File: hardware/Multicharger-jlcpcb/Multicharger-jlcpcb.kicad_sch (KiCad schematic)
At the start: 27 parts, among them J101 Conn_01x02, J102 Conn_01x02, J103 Tagbase, J104 USB_B_Mini, SW101 SW_DIP_x04, U101 TPS3700, U106 XC6206-3.3V

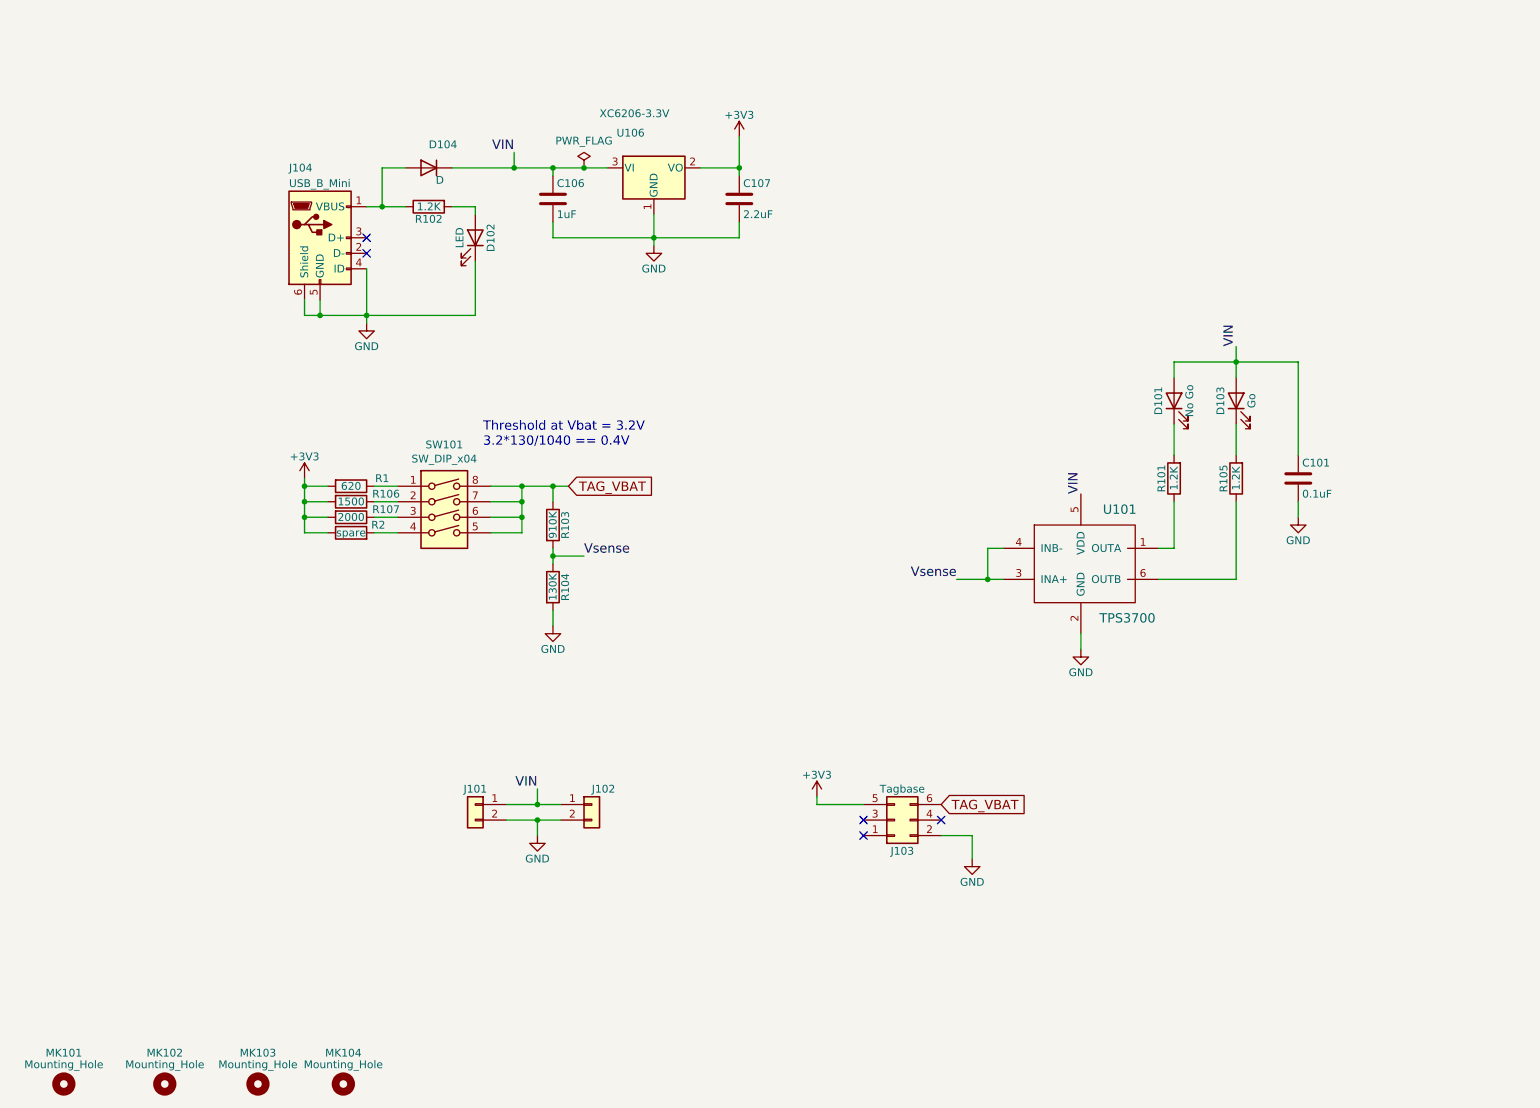
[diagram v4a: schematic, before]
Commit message: update multicharger to use basic parts
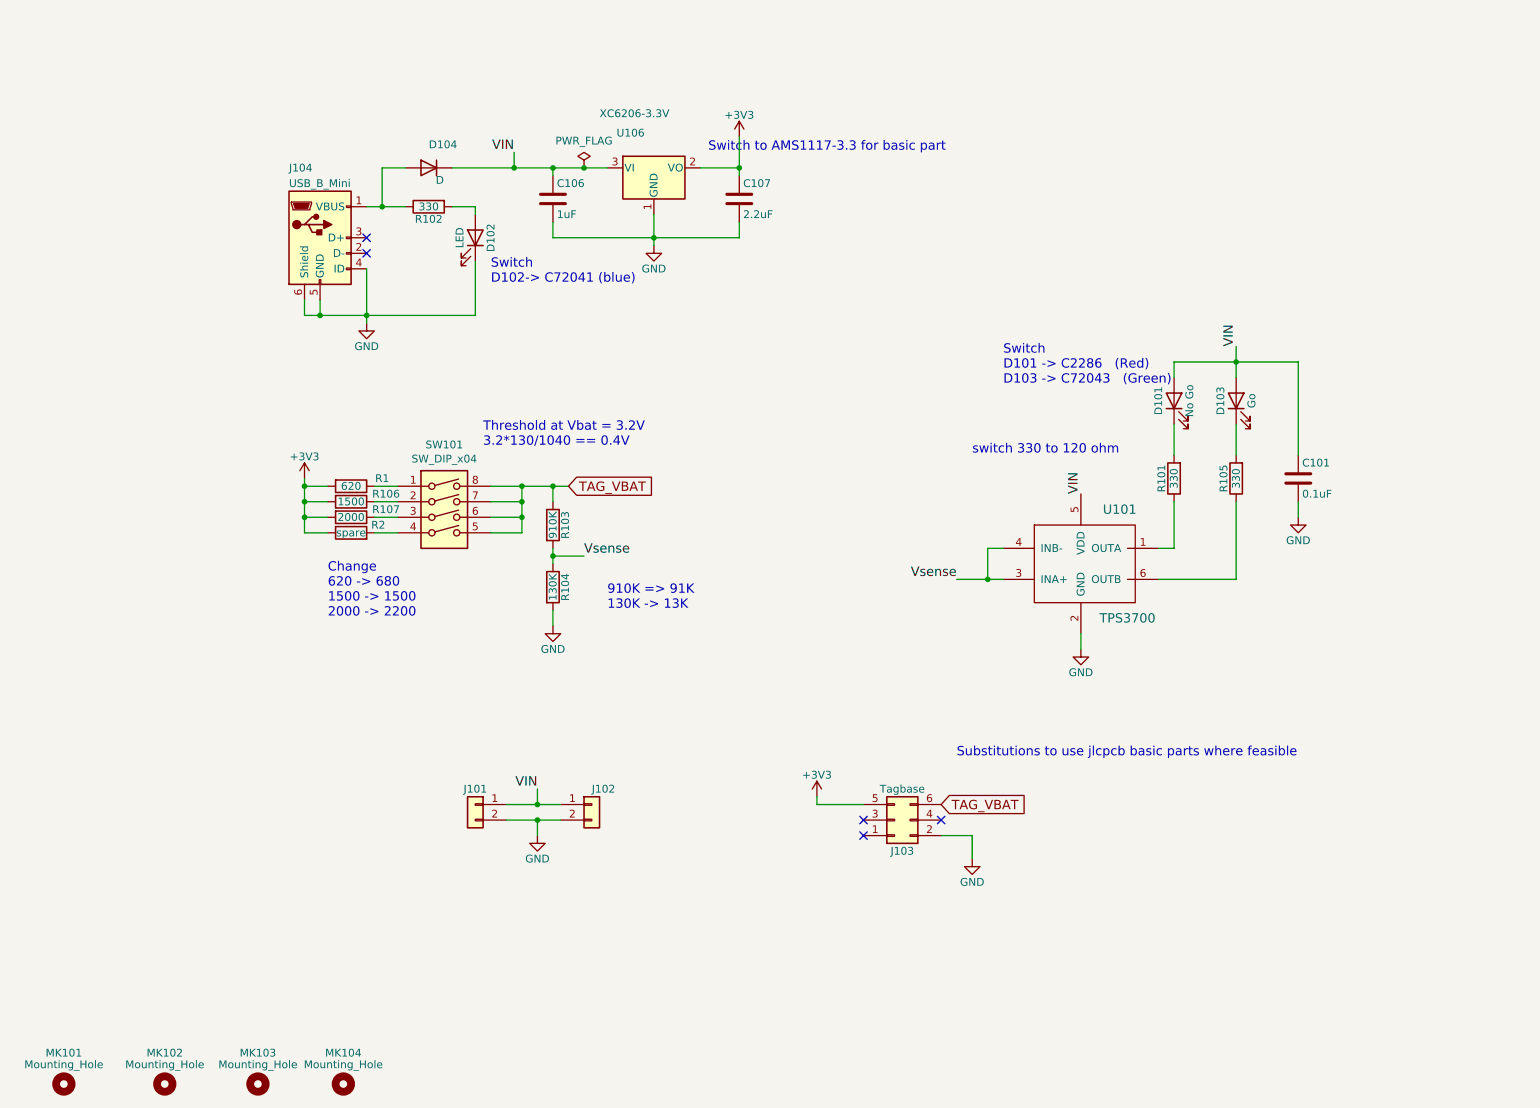
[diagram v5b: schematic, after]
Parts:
- R101, R102, R105: value 1.2K -> 330; LCSC C114605 -> C23138; MFN Yaego -> Uniroyal; MPN RC0603FR-071K2L -> 0603WAF3300T5E
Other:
- note added: "910K => 91K 130K -> 13K"
- note added: "Change 620 -> 680 1500 -> 1500 2000 -> 2200"
- note added: "Substitutions to use jlcpcb basic parts where feasible"
- note added: "Switch D101 -> C2286 (Red) D103 -> C72043 (Green)"
- note added: "Switch D102-> C72041 (blue)"
- note added: "Switch to AMS1117-3.3 for basic part"
- note added: "switch 330 to 120 ohm"
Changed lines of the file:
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@@
     (stroke (width 0) (type default) (color 0 0 0 0))
   )
+  (text "910K => 91K\n130K -> 13K" (at 125.73 114.3 0)
+    (effects (font (size 1.524 1.524)) (justify left bottom))
+  )
+  (text "Switch\nD102-> C72041 (blue)" (at 106.68 60.96 0)
+    (effects (font (size 1.524 1.524)) (justify left bottom))
+  )
   (text "Threshold at Vbat = 3.2V\n3.2*130/1040 == 0.4V" (at 105.41 87.63 0)
+    (effects (font (size 1.524 1.524)) (justify left bottom))
+  )
+  (text "switch 330 to 120 ohm\n" (at 185.42 88.9 0)
+    (effects (font (size 1.524 1.524)) (justify left bottom))
+  )
+  (text "Substitutions to use jlcpcb basic parts where feasible"
+    (at 182.88 138.43 0)
+    (effects (font (size 1.524 1.524)) (justify left bottom))
+  )
+  (text "Switch \nD101 -> C2286   (Red)\nD103 -> C72043   (Green)\n"
+    (at 190.5 77.47 0)
+    (effects (font (size 1.524 1.524)) (justify left bottom))
+  )
+  (text "Switch to AMS1117-3.3 for basic part" (at 142.24 39.37 0)
+    (effects (font (size 1.524 1.524)) (justify left bottom))
+  )
+  (text "Change\n620 -> 680\n1500 -> 1500\n2000 -> 2200\n" (at 80.01 115.57 0)
     (effects (font (size 1.524 1.524)) (justify left bottom))
   )
@@
     (in_bom yes) (on_board yes)
     (property "Reference" "R102" (id 0) (at 96.52 50.292 90))
-    (property "Value" "1.2K" (id 1) (at 96.52 48.26 90))
+    (property "Value" "330" (id 1) (at 96.52 48.26 90))
     (property "Footprint" "Resistor_SMD:R_0603_1608Metric" (id 2) (at 96.52 46.482 90)
       (effects (font (size 1.27 1.27)) hide)
@@
       (effects (font (size 1.27 1.27)) hide)
     )
-    (property "MPN" "RC0603FR-071K2L" (id 4) (at 96.52 48.26 90)
-      (effects (font (size 1.27 1.27)) hide)
-    )
-    (property "MFN" "Yaego" (id 6) (at 96.52 48.26 0)
-      (effects (font (size 1.27 1.27)) hide)
-    )
-    (property "Description" "RES SMD 1.2K OHM 5% 1/16W " (id 7) (at 96.52 48.26 0)
-      (effects (font (size 1.27 1.27)) hide)
-    )
-    (property "LCSC" "C114605" (id 8) (at 96.52 48.26 90)
+    (property "MPN" "0603WAF3300T5E" (id 4) (at 96.52 48.26 90)
+      (effects (font (size 1.27 1.27)) hide)
+    )
+    (property "MFN" "Uniroyal" (id 6) (at 96.52 48.26 0)
+      (effects (font (size 1.27 1.27)) hide)
+    )
+    (property "Description" "100mW Thick Film Resistors ±100ppm/℃ ±1% 330Ω 0603 " (id 7) (at 96.52 48.26 0)
+      (effects (font (size 1.27 1.27)) hide)
+    )
+    (property "LCSC" "C23138" (id 8) (at 96.52 48.26 90)
       (effects (font (size 1.524 1.524)) hide)
     )
@@
     (in_bom yes) (on_board yes)
     (property "Reference" "R105" (id 0) (at 226.568 92.71 90))
-    (property "Value" "1.2K" (id 1) (at 228.6 92.71 90))
+    (property "Value" "330" (id 1) (at 228.6 92.71 90))
     (property "Footprint" "Resistor_SMD:R_0603_1608Metric" (id 2) (at 230.378 92.71 90)
       (effects (font (size 1.27 1.27)) hide)
@@
       (effects (font (size 1.27 1.27)) hide)
     )
-    (property "MPN" "RC0603FR-071K2L" (id 4) (at 228.6 92.71 90)
-      (effects (font (size 1.27 1.27)) hide)
-    )
-    (property "MFN" "Yaego" (id 6) (at 228.6 92.71 0)
-      (effects (font (size 1.27 1.27)) hide)
-    )
-    (property "Description" "RES SMD 1.2K OHM 5% 1/16W " (id 7) (at 228.6 92.71 0)
+    (property "MPN" "0603WAF3300T5E" (id 4) (at 228.6 92.71 90)
+      (effects (font (size 1.27 1.27)) hide)
+    )
+    (property "MFN" "Uniroyal" (id 6) (at 228.6 92.71 0)
+      (effects (font (size 1.27 1.27)) hide)
+    )
+    (property "Description" "100mW Thick Film Resistors ±100ppm/℃ ±1% 330Ω 0603 " (id 7) (at 228.6 92.71 0)
       (effects (font (size 1.27 1.27)) hide)
     )
@@
       (effects (font (size 1.524 1.524)) hide)
     )
-    (property "LCSC" "C114605" (id 9) (at 228.6 92.71 0)
+    (property "LCSC" "C23138" (id 9) (at 228.6 92.71 0)
       (effects (font (size 1.27 1.27)) hide)
     )
@@
     (in_bom yes) (on_board yes)
     (property "Reference" "R101" (id 0) (at 216.408 92.71 90))
-    (property "Value" "1.2K" (id 1) (at 218.44 92.71 90))
+    (property "Value" "330" (id 1) (at 218.44 92.71 90))
     (property "Footprint" "Resistor_SMD:R_0603_1608Metric" (id 2) (at 220.218 92.71 90)
       (effects (font (size 1.27 1.27)) hide)
@@
       (effects (font (size 1.27 1.27)) hide)
     )
-    (property "MPN" "RC0603FR-071K2L" (id 4) (at 218.44 92.71 90)
-      (effects (font (size 1.27 1.27)) hide)
-    )
-    (property "MFN" "Yaego" (id 6) (at 218.44 92.71 0)
-      (effects (font (size 1.27 1.27)) hide)
-    )
-    (property "Description" "RES SMD 1.2K OHM 5% 1/16W " (id 7) (at 218.44 92.71 0)
-      (effects (font (size 1.27 1.27)) hide)
-    )
-    (property "LCSC" "C114605" (id 8) (at 218.44 92.71 90)
+    (property "MPN" "0603WAF3300T5E" (id 4) (at 218.44 92.71 90)
+      (effects (font (size 1.27 1.27)) hide)
+    )
+    (property "MFN" "Uniroyal" (id 6) (at 218.44 92.71 0)
+      (effects (font (size 1.27 1.27)) hide)
+    )
+    (property "Description" "100mW Thick Film Resistors ±100ppm/℃ ±1% 330Ω 0603 " (id 7) (at 218.44 92.71 0)
+      (effects (font (size 1.27 1.27)) hide)
+    )
+    (property "LCSC" "C23138" (id 8) (at 218.44 92.71 90)
       (effects (font (size 1.524 1.524)) hide)
     )
@@
     )
     (path "/00000000-0000-0000-0000-00005b72d71f"
-      (reference "R101") (unit 1) (value "1.2K") (footprint "Resistor_SMD:R_0603_1608Metric")
+      (reference "R101") (unit 1) (value "330") (footprint "Resistor_SMD:R_0603_1608Metric")
     )
     (path "/00000000-0000-0000-0000-00005b06b8b2"
-      (reference "R102") (unit 1) (value "1.2K") (footprint "Resistor_SMD:R_0603_1608Metric")
+      (reference "R102") (unit 1) (value "330") (footprint "Resistor_SMD:R_0603_1608Metric")
     )
     (path "/00000000-0000-0000-0000-00005b72cf14"
@@
     )
     (path "/00000000-0000-0000-0000-00005b72d633"
-      (reference "R105") (unit 1) (value "1.2K") (footprint "Resistor_SMD:R_0603_1608Metric")
+      (reference "R105") (unit 1) (value "330") (footprint "Resistor_SMD:R_0603_1608Metric")
     )
     (path "/00000000-0000-0000-0000-00006111918b"

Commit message: checkpoint
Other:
- note added: "Switch to AMS1117-3.3 for basic part NB Need either a schottky diode or a regulator with reverse current protection"
- note removed: "Switch to AMS1117-3.3 for basic part"
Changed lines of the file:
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@@
     (effects (font (size 1.524 1.524)) (justify left bottom))
   )
-  (text "Switch to AMS1117-3.3 for basic part" (at 142.24 39.37 0)
+  (text "Switch to AMS1117-3.3 for basic part\n\nNB Need either a schottky diode or a regulator with reverse current protection"
+    (at 142.24 39.37 0)
     (effects (font (size 1.524 1.524)) (justify left bottom))
   )

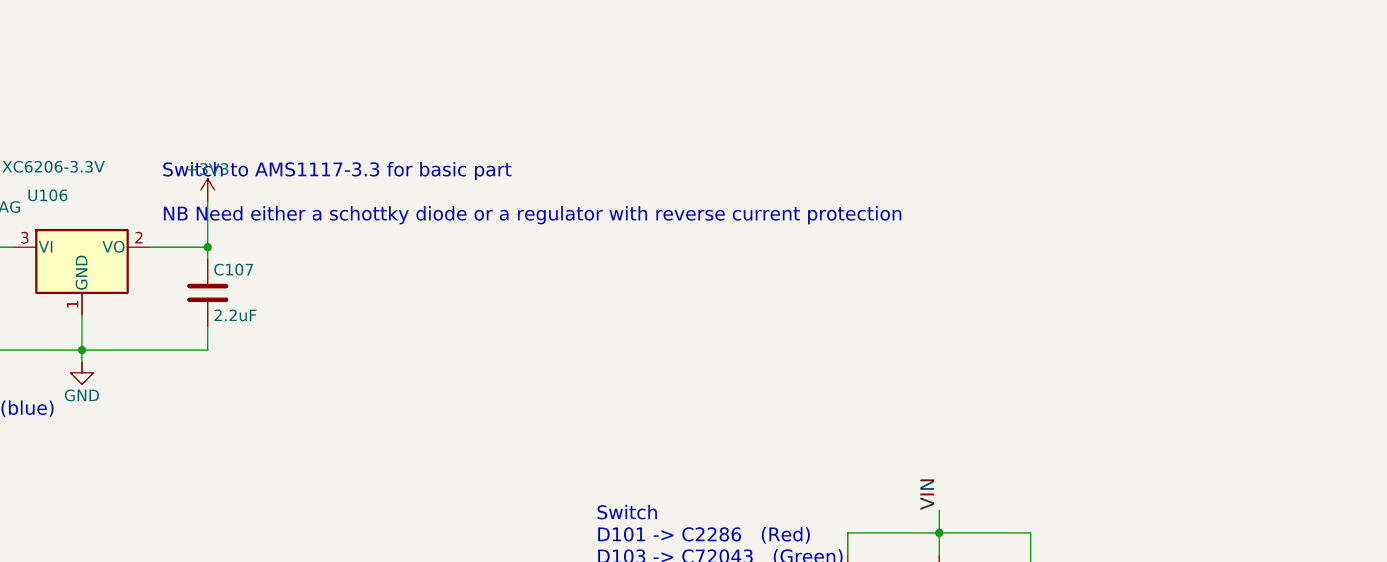
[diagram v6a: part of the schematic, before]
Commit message: added comments to multicharger
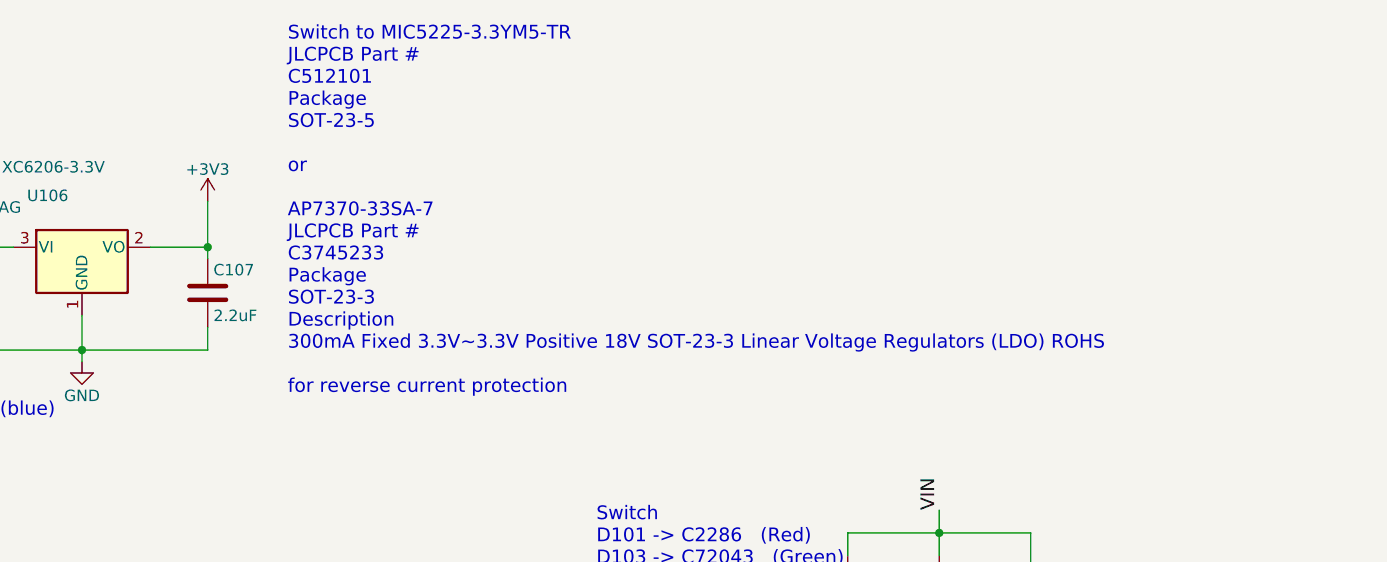
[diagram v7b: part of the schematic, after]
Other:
- note added: "Switch to MIC5225-3.3YM5-TR JLCPCB Part # C512101 Package SOT-23-5 or AP7370-33SA-7 JLCPCB Part # C3745233 Package SOT-23-3 Description 300mA Fixed 3.3V~3.3V Positive 18V SOT-23-3 Linear Voltage Regulators (LDO) ROHS for reverse current protection"
- note removed: "Switch to AMS1117-3.3 for basic part NB Need either a schottky diode or a regulator with reverse current protection"
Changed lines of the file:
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@@
     (effects (font (size 1.524 1.524)) (justify left bottom))
   )
-  (text "Switch to AMS1117-3.3 for basic part\n\nNB Need either a schottky diode or a regulator with reverse current protection"
-    (at 142.24 39.37 0)
+  (text "Switch to MIC5225-3.3YM5-TR\nJLCPCB Part #\nC512101\nPackage\nSOT-23-5\n\nor\n\nAP7370-33SA-7\nJLCPCB Part #\nC3745233\nPackage\nSOT-23-3\nDescription\n300mA Fixed 3.3V~3.3V Positive 18V SOT-23-3 Linear Voltage Regulators (LDO) ROHS\n\nfor reverse current protection"
+    (at 156.21 58.42 0)
     (effects (font (size 1.524 1.524)) (justify left bottom))
   )

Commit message: updated jlcpcb multicharger
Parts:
- removed D104: D, Diode_SMD:D_0402_1005Metric, symbol Device:D
- added D104, D105: D_Schottky, Diode_SMD:D_SOD-323, symbol Device:D_Schottky
- D101: value No Go -> No Go Red; LCSC C72041 -> C2286; MFN Everlight Elec -> Hubei KENTO Elec; MPN 19-217/BHC-ZL1M2RY/3T -> KT-0603R
- D102: value LED -> BLUE; C72041 (none) -> C72041; LCSC C72043 -> (none)
- D103: value Go -> Go Green
- R1: value 620 -> 680; LCSC C23220 -> C23228; MPN 0603WAF6200T5E -> 0603WAF6800T5E
- R101: value 330 -> 220; LCSC C23138 -> C22962; MPN 0603WAF3300T5E -> 0603WAF2200T5E
- R102, R105: value 330 -> 120; LCSC C23138 -> C22787; MPN 0603WAF3300T5E -> 0603WAF1200T5E
- R103: value 910K -> 91K; footprint Resistor_SMD:R_0402_1005Metric -> Resistor_SMD:R_0603_1608Metric; LCSC C137927 -> C23265; MFN Yageo -> Uniroyal; MPN FRC0603J914TS -> 0603WAF9102T5E
- R104: value 130K -> 13K; footprint Resistor_SMD:R_0402_1005Metric -> Resistor_SMD:R_0603_1608Metric; LCSC C93946 -> C22797; MFN Yageo -> Uniroyal; MPN RC0402FR-07910KL -> 0603WAF1302T5E
- R106: footprint Resistor_SMD:R_0402_1005Metric -> Resistor_SMD:R_0603_1608Metric; LCSC C144053 -> C22843; MFN Yageo -> Uniroyal; MPN AF0402JR-071K5L -> 0603WAF1501T5E
- R107: value 2000 -> 2.2K; footprint Resistor_SMD:R_0402_1005Metric -> Resistor_SMD:R_0603_1608Metric; LCSC C137887 -> 0603WAF2201T5E; MFN Yageo -> Uniroyal; MPN RC0402JR-072KL -> 0603WAF2201T5E
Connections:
- net VIN: now also D104.1 (K), D105.2 (A); no longer C106.1, U106.3 (VI)
- net at J104.1 (VBUS), R102.1: now also D104.2 (A)
- new net: C106.1, D105.1 (K), U106.3 (VI)
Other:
- note added: "RED LED 220 Green/Blue 110"
- note added: "Threshold at Vbat = 3.2V 3.2*13/104 == 0.4V"
- note removed: "910K => 91K 130K -> 13K"
- note removed: "Change 620 -> 680 1500 -> 1500 2000 -> 2200"
- note removed: "Switch D101 -> C2286 (Red) D103 -> C72043 (Green)"
- note removed: "Switch D102-> C72041 (blue)"
- note removed: "Switch to MIC5225-3.3YM5-TR JLCPCB Part # C512101 Package SOT-23-5 or AP7370-33SA-7 JLCPCB Part # C3745233 Package SOT-23-3 Description 300mA Fixed 3.3V~3.3V Positive 18V SOT-23-3 Linear Voltage Regulators (LDO) ROHS for reverse current protection"
- note removed: "Threshold at Vbat = 3.2V 3.2*130/1040 == 0.4V"
- note removed: "switch 330 to 120 ohm"
- title: Tag Charger -- multiple ms series batteries -> Tag Charger -- multiple ms series batteries -- jlcpcb
